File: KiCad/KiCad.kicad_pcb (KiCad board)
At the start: 2 copper layers, 4 parts, among them SW1 SW_Push, SW2 SW_Push, SW3 SW_Push, U1 MOUDLE-SEEEDUINO-XIAO

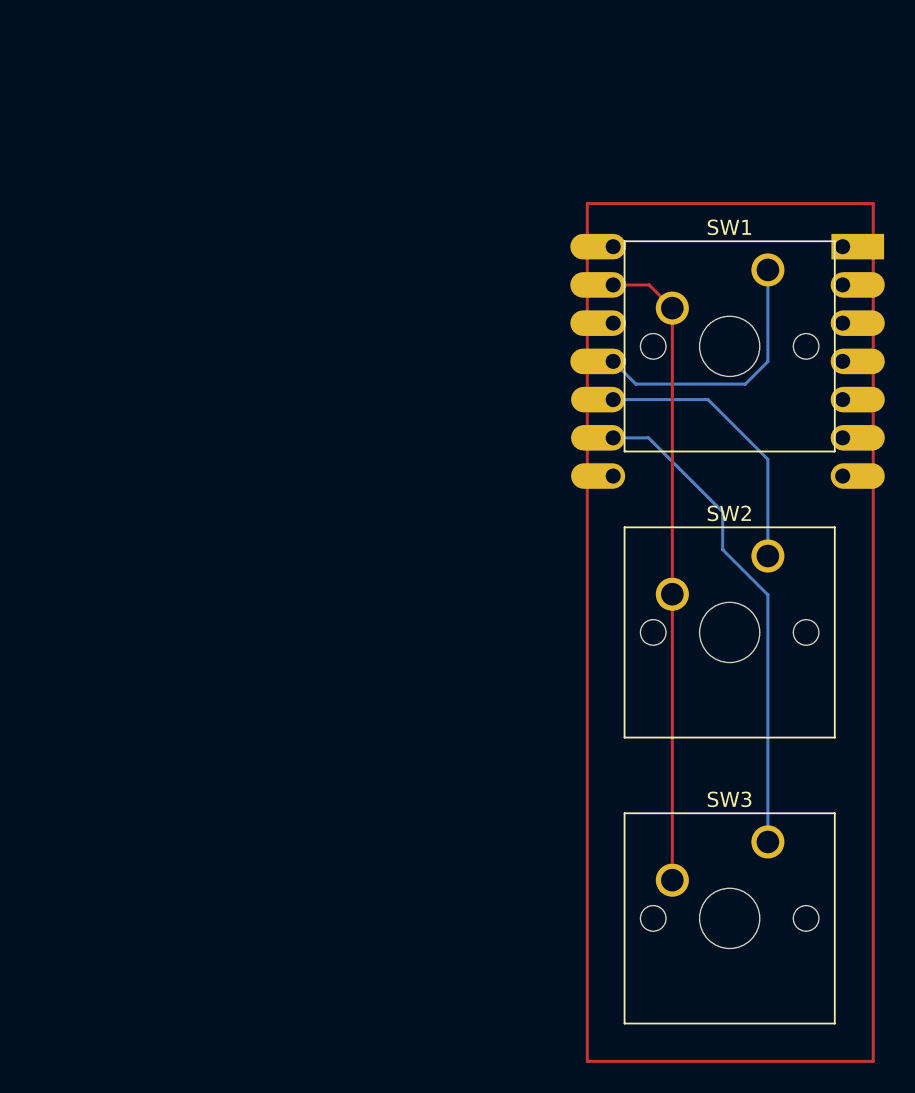
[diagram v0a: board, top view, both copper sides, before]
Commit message: Add rotary encoder and redesigned the case.
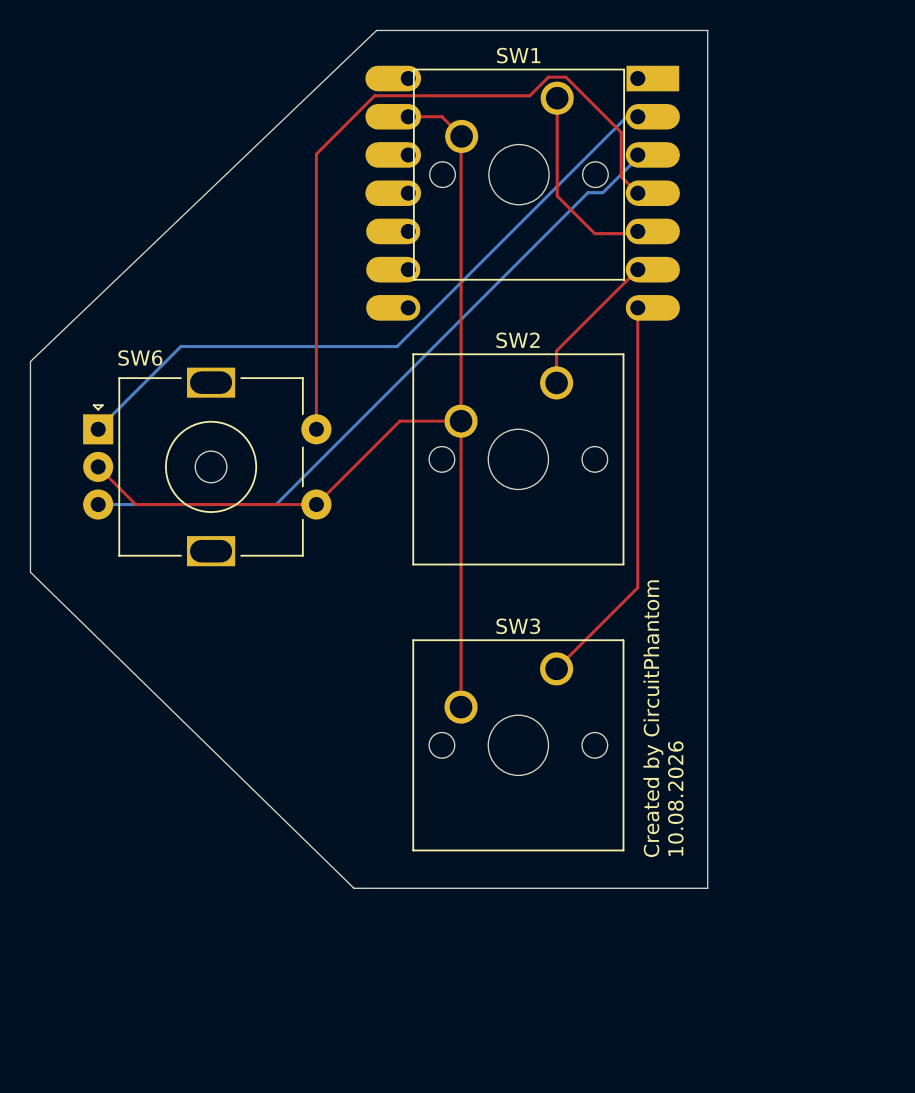
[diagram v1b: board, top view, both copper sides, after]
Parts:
- added SW6: RotaryEncoder_Switch, Rotary_Encoder:RotaryEncoder_Alps_EC11E-Switch_Vertical_H20mm_MountingHoles, F.Cu at (126.0, 97.5)
- moved SW2 18.1 mm to (156.5, 94.4)
- moved SW3 18.1 mm to (156.5, 113.4)
- moved SW1 18.1 mm to (156.5, 75.5)
- moved U1 17.6 mm to (154.2, 81.8)
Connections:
- SW1 pad 1: Net-(U1-PA6_A10_D10_MOSI) -> Net-(U1-PA8_A4_D4_SDA)
- SW2 pad 1: Net-(U1-PA5_A9_D9_MISO) -> Net-(U1-PA9_A5_D5_SCL)
- SW3 pad 1: Net-(U1-PA7_A8_D8_SCK) -> Net-(U1-PB08_A6_D6_TX)
- U1 pad 10: Net-(U1-PA5_A9_D9_MISO) -> unconnected-(U1-PA5_A9_D9_MISO-Pad10)
- U1 pad 11: Net-(U1-PA6_A10_D10_MOSI) -> unconnected-(U1-PA6_A10_D10_MOSI-Pad11)
- U1 pad 2: unconnected-(U1-PA4_A1_D1-Pad2) -> Net-(U1-PA4_A1_D1)
- U1 pad 3: unconnected-(U1-PA10_A2_D2-Pad3) -> Net-(U1-PA10_A2_D2)
- U1 pad 4: unconnected-(U1-PA11_A3_D3-Pad4) -> Net-(U1-PA11_A3_D3)
- U1 pad 5: unconnected-(U1-PA8_A4_D4_SDA-Pad5) -> Net-(U1-PA8_A4_D4_SDA)
- U1 pad 6: unconnected-(U1-PA9_A5_D5_SCL-Pad6) -> Net-(U1-PA9_A5_D5_SCL)
- U1 pad 7: unconnected-(U1-PB08_A6_D6_TX-Pad7) -> Net-(U1-PB08_A6_D6_TX)
- U1 pad 9: Net-(U1-PA7_A8_D8_SCK) -> unconnected-(U1-PA7_A8_D8_SCK-Pad9)
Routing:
- net Net-(U1-PA11_A3_D3): track 0.00 -> 46.7 mm
- net Net-(U1-PA10_A2_D2): track 0.00 -> 45.6 mm
- net Net-(U1-PA4_A1_D1): track 0.00 -> 44.5 mm
- net Net-(U1-PA7_A8_D8_SCK): track 32.5 -> 0.00 mm
- net GND: track 42.6 -> 69.5 mm
- net Net-(U1-PB08_A6_D6_TX): track 0.00 -> 26.2 mm
- net Net-(U1-PA5_A9_D9_MISO): track 18.3 -> 0.00 mm
- net Net-(U1-PA6_A10_D10_MOSI): track 17.6 -> 0.00 mm
- net Net-(U1-PA8_A4_D4_SDA): track 0.00 -> 13.0 mm
- net Net-(U1-PA9_A5_D5_SCL): track 0.00 -> 9.76 mm
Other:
- board outline added: 45 x 57 mm
- board text added: "Created by CircuitPhantom 10.08.2026"

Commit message: Changed the case, add assembly model. Fixed PCB design.
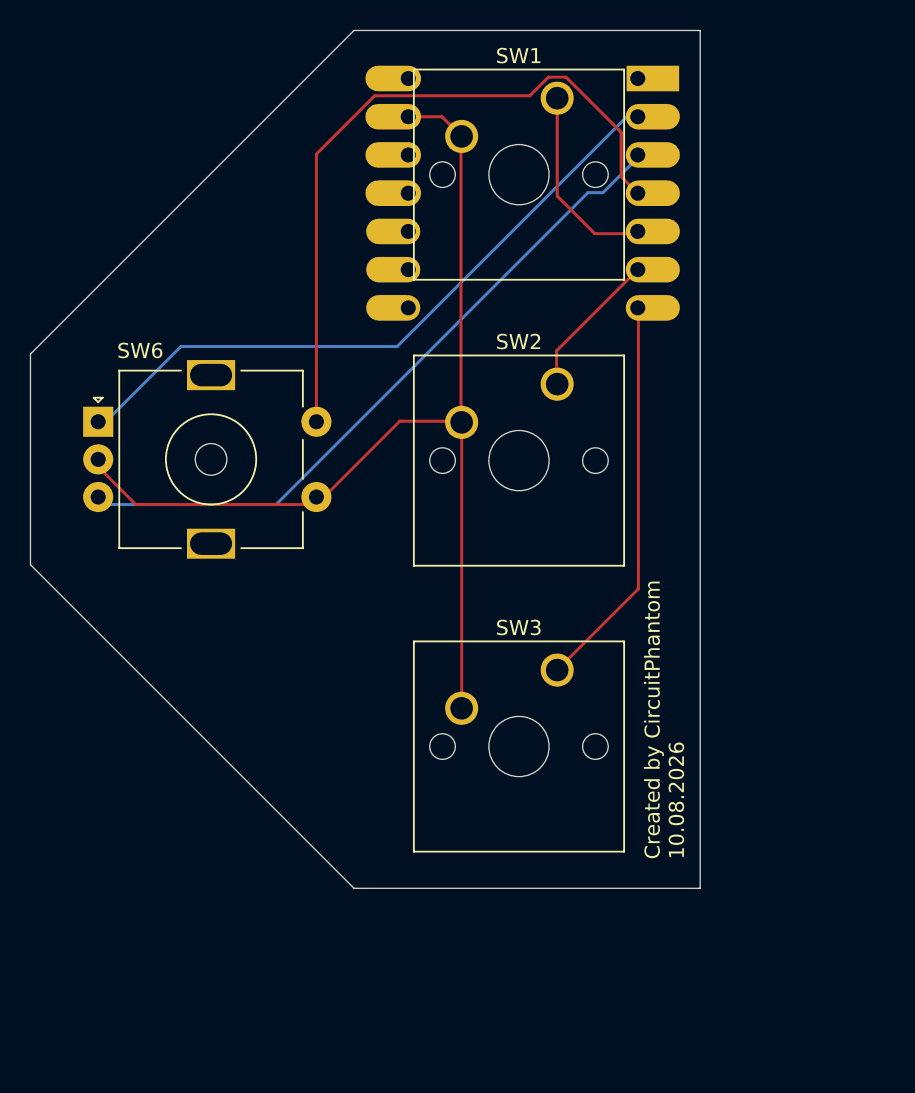
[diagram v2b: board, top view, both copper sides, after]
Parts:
- moved SW6 0.50 mm to (126.0, 97.0)
- moved SW2 0.09 mm to (156.5, 94.5)
- moved SW3 0.09 mm to (156.5, 113.5)
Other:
- board size 45 x 57 mm -> 44.5 x 57 mm
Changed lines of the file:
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@@
 	(footprint "Button_Switch_Keyboard:SW_Cherry_MX_1.00u_PCB"
 		(layer "F.Cu")
-		(at 156.46 113.42)
+		(at 156.5 113.5)
 		(descr "Cherry MX keyswitch, 1.00u, PCB mount, http://cherryamericas.com/wp-content/uploads/2014/12/mx_cat.pdf")
 		(tags "Cherry MX keyswitch 1.00u PCB")
@@
 	(footprint "Button_Switch_Keyboard:SW_Cherry_MX_1.00u_PCB"
 		(layer "F.Cu")
-		(at 156.46 94.42)
+		(at 156.5 94.5)
 		(descr "Cherry MX keyswitch, 1.00u, PCB mount, http://cherryamericas.com/wp-content/uploads/2014/12/mx_cat.pdf")
 		(tags "Cherry MX keyswitch 1.00u PCB")
@@
 	(footprint "Rotary_Encoder:RotaryEncoder_Alps_EC11E-Switch_Vertical_H20mm_MountingHoles"
 		(layer "F.Cu")
-		(at 126 97.5)
+		(at 126 97)
 		(descr "Alps rotary encoder, EC11E... with switch, vertical shaft, https://www.lcsc.com/datasheet/lcsc_datasheet_2410010003_ALPSALPINE-EC11E09444A8_C1322538.pdf")
 		(tags "rotary encoder")
@@
 	)
 	(gr_line
-		(start 121.5 93)
-		(end 144.5 71)
+		(start 121.5 92.5)
+		(end 143 71)
 		(stroke
 			(width 0.05)
@@
 	)
 	(gr_line
-		(start 121.5 107)
-		(end 121.5 93)
+		(start 121.5 106.5)
+		(end 121.5 92.5)
 		(stroke
 			(width 0.05)
@@
 	)
 	(gr_line
-		(start 143 128)
-		(end 121.5 107)
+		(start 143 71)
+		(end 166 71)
 		(stroke
 			(width 0.05)
@@
 	)
 	(gr_line
-		(start 144.5 71)
-		(end 166.5 71)
+		(start 143 128)
+		(end 121.5 106.5)
 		(stroke
 			(width 0.05)
@@
 	)
 	(gr_line
-		(start 166.5 71)
-		(end 166.5 128)
+		(start 143 128)
+		(end 166 128)
 		(stroke
 			(width 0.05)
@@
 	)
 	(gr_line
-		(start 166.5 128)
-		(end 143 128)
+		(start 166 71)
+		(end 166 128)
 		(stroke
 			(width 0.05)
@@
 	)
 	(gr_text "Created by CircuitPhantom\n10.08.2026"
-		(at 165 126 90)
+		(at 165.04 126.08 90)
 		(layer "F.SilkS")
 		(effects
@@
 	)
 	(segment
+		(start 161.894 108.106)
+		(end 161.894 89.51253)
+		(width 0.2)
+		(layer "F.Cu")
+		(net "Net-(U1-PB08_A6_D6_TX)")
+	)
+	(segment
+		(start 156.5 113.5)
+		(end 161.894 108.106)
+		(width 0.2)
+		(layer "F.Cu")
+		(net "Net-(U1-PB08_A6_D6_TX)")
+	)
+	(segment
 		(start 128.5 102.5)
 		(end 140.5 102.5)
@@
 	)
 	(segment
-		(start 150.11 96.96)
-		(end 150.11 115.96)
+		(start 150.15 97.04)
+		(end 150.15 116.04)
 		(width 0.2)
 		(layer "F.Cu")
@@
 	)
 	(segment
-		(start 159 84.5)
-		(end 161.70653 84.5)
-		(width 0.2)
-		(layer "F.Cu")
-		(net "Net-(U1-PA8_A4_D4_SDA)")
-	)
-	(segment
-		(start 161.70653 84.5)
-		(end 161.854 84.35253)
-		(width 0.2)
-		(layer "F.Cu")
-		(net "Net-(U1-PA8_A4_D4_SDA)")
-	)
-	(segment
-		(start 156.5 75.5)
-		(end 156.5 82)
-		(width 0.2)
-		(layer "F.Cu")
-		(net "Net-(U1-PA8_A4_D4_SDA)")
-	)
-	(segment
-		(start 156.5 82)
-		(end 159 84.5)
-		(width 0.2)
-		(layer "F.Cu")
-		(net "Net-(U1-PA8_A4_D4_SDA)")
-	)
-	(segment
 		(start 156.46 92.28653)
 		(end 161.854 86.89253)
@@
 	)
 	(segment
-		(start 161.854 108.026)
-		(end 161.854 89.43253)
-		(width 0.2)
-		(layer "F.Cu")
-		(net "Net-(U1-PB08_A6_D6_TX)")
-	)
-	(segment
-		(start 156.46 113.42)
-		(end 161.854 108.026)
-		(width 0.2)
-		(layer "F.Cu")
-		(net "Net-(U1-PB08_A6_D6_TX)")
-	)
-	(segment
 		(start 145.863402 92)
 		(end 161.130872 76.73253)
@@
 	)
 	(segment
+		(start 161.854 79.463056)
+		(end 159.537056 81.78)
+		(width 0.2)
+		(layer "B.Cu")
+		(net "Net-(U1-PA10_A2_D2)")
+	)
+	(segment
 		(start 159.537056 81.78)
-		(end 161.854 79.463056)
+		(end 158.542944 81.78)
 		(width 0.2)
 		(layer "B.Cu")
@@
 	)
 	(segment
-		(start 161.854 79.463056)
-		(end 161.854 79.27253)
+		(start 161.854 79.27253)
+		(end 161.854 79.463056)
 		(width 0.2)
 		(layer "B.Cu")
@@
 	)
 	(segment
-		(start 137.822944 102.5)
-		(end 158.542944 81.78)
+		(start 126.5 102.5)
+		(end 126 102)
 		(width 0.2)
 		(layer "B.Cu")
@@
 	)
 	(segment
-		(start 126 102.5)
-		(end 137.822944 102.5)
+		(start 137.822944 102.5)
+		(end 126.5 102.5)
 		(width 0.2)
 		(layer "B.Cu")
@@
 	(segment
 		(start 158.542944 81.78)
-		(end 159.537056 81.78)
+		(end 137.822944 102.5)
 		(width 0.2)
 		(layer "B.Cu")
@@
 		(net "Net-(U1-PA11_A3_D3)")
 	)
+	(segment
+		(start 159 84.5)
+		(end 161.70653 84.5)
+		(width 0.2)
+		(layer "F.Cu")
+		(net "Net-(U1-PA8_A4_D4_SDA)")
+	)
+	(segment
+		(start 161.70653 84.5)
+		(end 161.854 84.35253)
+		(width 0.2)
+		(layer "F.Cu")
+		(net "Net-(U1-PA8_A4_D4_SDA)")
+	)
+	(segment
+		(start 156.5 75.5)
+		(end 156.5 82)
+		(width 0.2)
+		(layer "F.Cu")
+		(net "Net-(U1-PA8_A4_D4_SDA)")
+	)
+	(segment
+		(start 156.5 82)
+		(end 159 84.5)
+		(width 0.2)
+		(layer "F.Cu")
+		(net "Net-(U1-PA8_A4_D4_SDA)")
+	)
 	(embedded_fonts no)
